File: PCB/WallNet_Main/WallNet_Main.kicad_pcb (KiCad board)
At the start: 2 copper layers, 54 parts, among them J1 Conn_01x05_Pin, J101 USB_C_Receptacle_PowerOnly_6P, J102 Conn_01x04_Pin, J201 Conn_01x04_Pin, J202 Conn_01x07_Socket, J203 Conn_02x12_Counter_Clockwise, Q201 BSS138, SW1 SW, SW201 SW, U1 BT832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

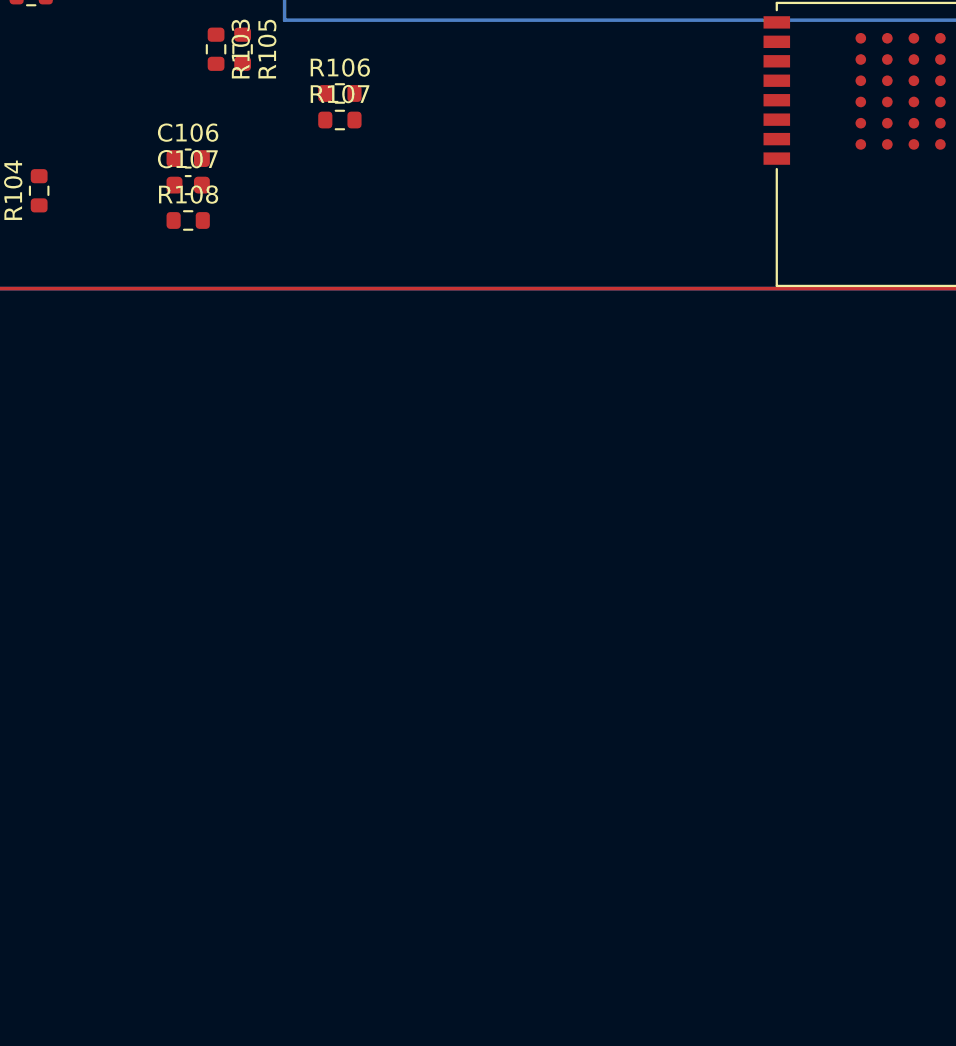
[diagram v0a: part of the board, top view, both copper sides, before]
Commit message: "added test point debugging and mounting holes"
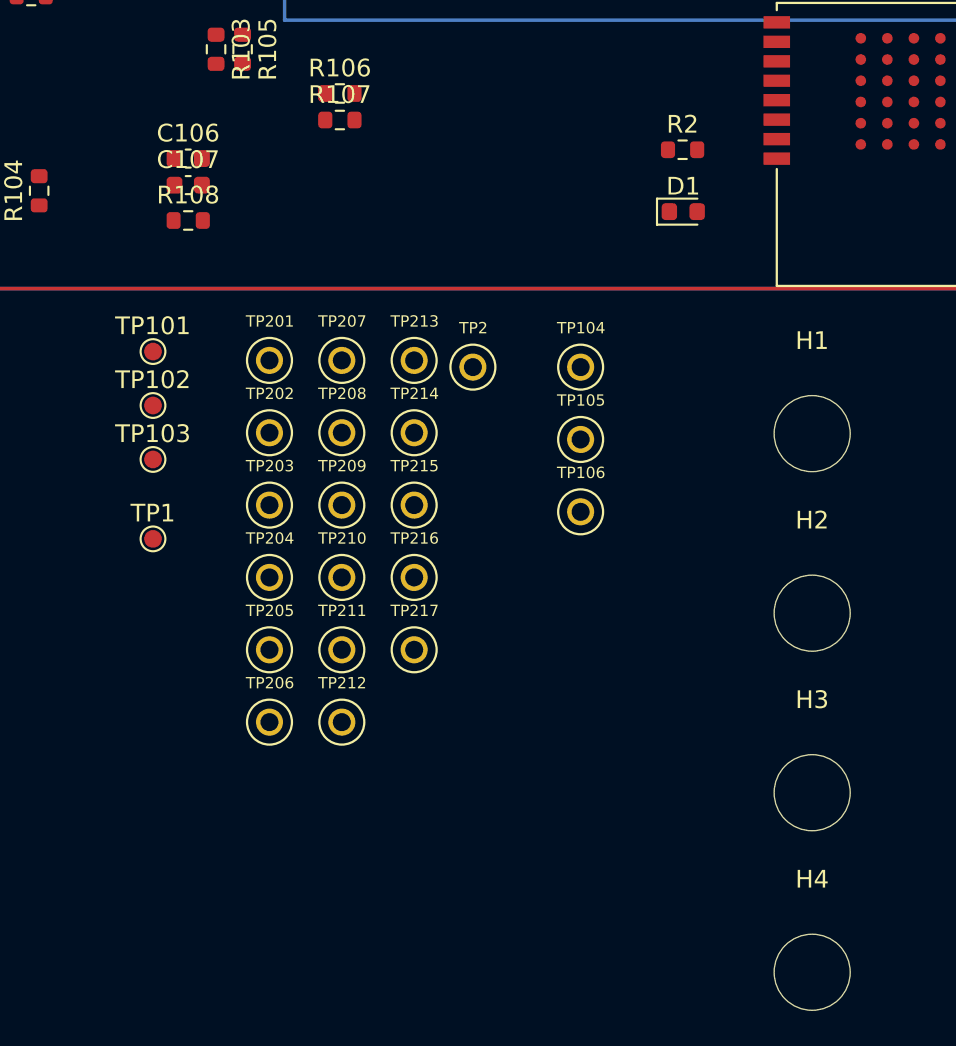
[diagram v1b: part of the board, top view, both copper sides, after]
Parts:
- added D1: LED, Diode_SMD:D_0603_1608Metric, F.Cu at (101.2, 115.5)
- added H1: MountingHole, MountingHole:MountingHole_4.3mm_M4, F.Cu at (108.5, 128.1)
- added H2: MountingHole, MountingHole:MountingHole_4.3mm_M4, F.Cu at (108.5, 138.2)
- added H3: MountingHole, MountingHole:MountingHole_4.3mm_M4, F.Cu at (108.5, 148.3)
- added H4: MountingHole, MountingHole:MountingHole_4.3mm_M4, F.Cu at (108.5, 158.5)
- added R2: 240, Resistor_SMD:R_0603_1608Metric, F.Cu at (101.2, 112.0)
- added TP1: GND, TestPoint:TestPoint_Pad_D1.0mm, F.Cu at (71.2, 134.0)
- added TP101: VBat, TestPoint:TestPoint_Pad_D1.0mm, F.Cu at (71.2, 123.4)
- added TP102: VUSB, TestPoint:TestPoint_Pad_D1.0mm, F.Cu at (71.2, 126.5)
- added TP103: VSys, TestPoint:TestPoint_Pad_D1.0mm, F.Cu at (71.2, 129.5)
- added TP104: BQ_SDA, 5001:KEYSTONE_5001, F.Cu at (95.4, 124.3)
- added TP105: BQ_SCL, 5001:KEYSTONE_5001, F.Cu at (95.4, 128.4)
- added TP106: BQ_INT, 5001:KEYSTONE_5001, F.Cu at (95.4, 132.5)
- added TP2: GND, 5001:KEYSTONE_5001, F.Cu at (89.3, 124.3)
- added TP201: TS_TX, 5001:KEYSTONE_5001, F.Cu at (77.8, 123.9)
- added TP202: TS_RX, 5001:KEYSTONE_5001, F.Cu at (77.8, 128.0)
- added TP203: GPS_SDA, 5001:KEYSTONE_5001, F.Cu at (77.8, 132.1)
- added TP204: GPS_SCL, 5001:KEYSTONE_5001, F.Cu at (77.8, 136.2)
- added TP205: GPS_INT, 5001:KEYSTONE_5001, F.Cu at (77.8, 140.3)
- added TP206: GPS_TP, 5001:KEYSTONE_5001, F.Cu at (77.8, 144.4)
- added TP207: RFID_RST, 5001:KEYSTONE_5001, F.Cu at (81.9, 123.9)
- added TP208: RFID_SCK, 5001:KEYSTONE_5001, F.Cu at (81.9, 128.0)
- added TP209: RFID_MISO, 5001:KEYSTONE_5001, F.Cu at (81.9, 132.1)
- added TP210: RFID_MOSI, 5001:KEYSTONE_5001, F.Cu at (81.9, 136.2)
- added TP211: RFID_SS, 5001:KEYSTONE_5001, F.Cu at (81.9, 140.3)
- added TP212: EP_DC, 5001:KEYSTONE_5001, F.Cu at (81.9, 144.4)
- added TP213: EP_SDA, 5001:KEYSTONE_5001, F.Cu at (86.0, 123.9)
- added TP214: EP_SCL, 5001:KEYSTONE_5001, F.Cu at (86.0, 128.0)
- added TP215: EP_CSB, 5001:KEYSTONE_5001, F.Cu at (86.0, 132.1)
- added TP216: EP_BUSY, 5001:KEYSTONE_5001, F.Cu at (86.0, 136.2)
- added TP217: EP_RESET, 5001:KEYSTONE_5001, F.Cu at (86.0, 140.3)
- R109: value UNKNOWN -> 240

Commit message: Updated, Schematic done, waiting on Layout
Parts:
- removed SW201: SW, 436331045822:4363X10458XX
- added L101: 2.2uH, ISMC:IND_IMSC1008AZER_VIS, F.Cu at (46.2, 91.4)
- added L201: 68uH, VLS3015CX_680M_H:IND_VLS3015CX-680M-H, F.Cu at (184.2, 74.8)
- added S201: 436331045822, 436331045822:4363X10458XX, F.Cu at (156.8, 66.2)
- moved TP211 188.4 mm to (239.9, 37.6)
- moved TP210 182.0 mm to (234.9, 37.6)
- moved TP209 175.2 mm to (229.4, 37.6)
- moved TP208 168.3 mm to (223.9, 37.6)
- moved H2 165.6 mm to (274.0, 133.5)
- moved H3 165.5 mm to (274.0, 146.3)
- moved H4 165.5 mm to (274.0, 156.5)
- moved H1 165.2 mm to (273.5, 120.0)
- moved TP207 161.9 mm to (218.9, 37.6)
- moved TP206 153.5 mm to (190.9, 40.6)
- moved TP205 147.4 mm to (186.4, 40.6)
- moved TP204 141.3 mm to (181.9, 40.6)
- moved TP212 138.7 mm to (205.2, 80.8)
- moved TP203 135.2 mm to (177.4, 40.6)
- moved C202 129.8 mm to (193.2, 55.2)
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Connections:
- J102 pad MP: (no net) -> GND
- J201 pad MP: (no net) -> GND
- J203 pad MP: (no net) -> GND

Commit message: Placed components on board
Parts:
- moved H4 292.0 mm to (17.5, 17.0)
- moved H3 265.8 mm to (17.5, 76.5)
- moved TP211 220.9 mm to (19.5, 52.0)
- moved J202 219.1 mm to (20.8, 56.0), turned to 0 degrees
- moved TP210 215.0 mm to (24.0, 79.5)
- moved TP209 208.9 mm to (24.0, 75.5)
- moved TP208 200.3 mm to (28.0, 79.5)
- moved TP207 199.7 mm to (19.5, 48.5)
- moved U201 178.6 mm to (67.5, 17.0)
- moved H1 178.3 mm to (128.0, 17.0)
- moved H2 156.7 mm to (128.0, 76.5)
- moved C1 128.6 mm to (25.3, 15.0), turned to 180 degrees
- moved C3 124.5 mm to (25.9, 17.8), turned to 180 degrees
- moved D1 121.6 mm to (29.8, 15.0), turned to 180 degrees
- moved R2 117.2 mm to (29.8, 18.5), turned to 180 degrees
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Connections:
- J102 pad MP: GND -> (no net)
- J201 pad MP: GND -> (no net)
- J203 pad MP: GND -> (no net)

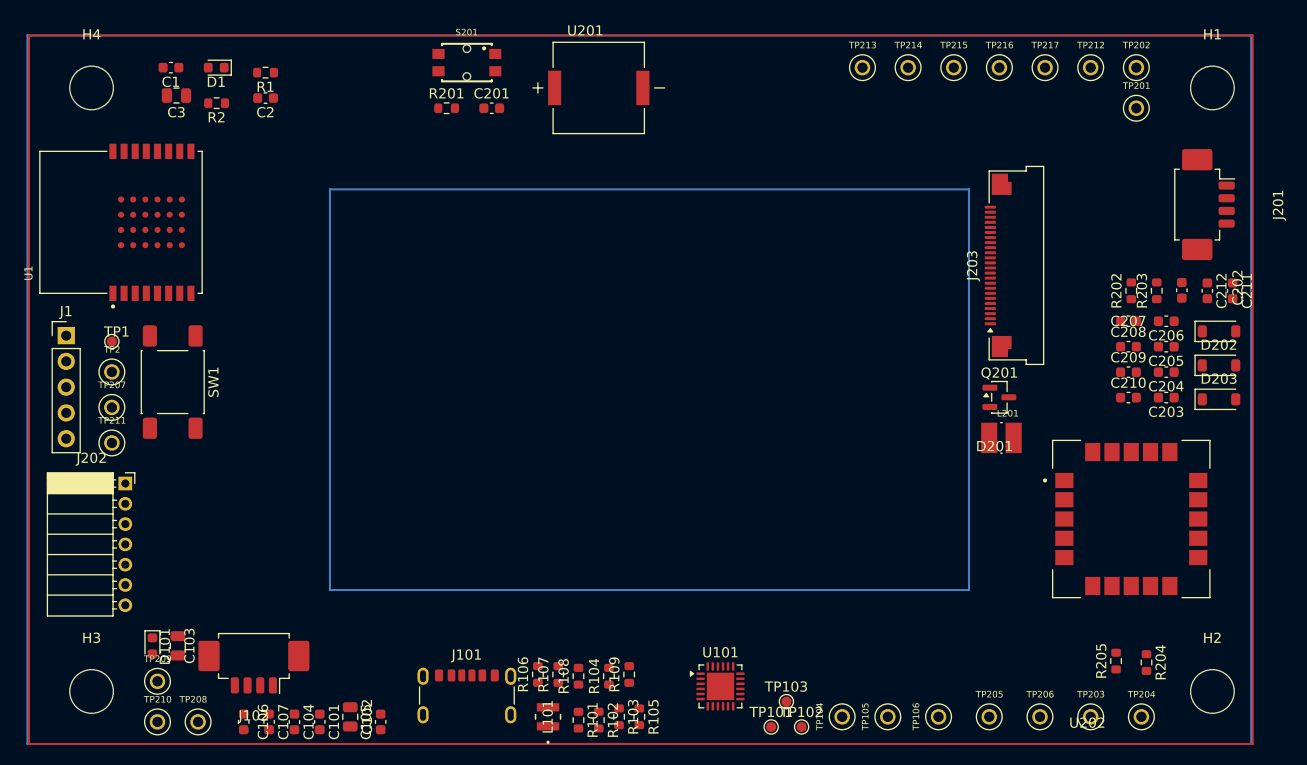
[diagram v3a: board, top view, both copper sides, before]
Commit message: Added some of the power traces
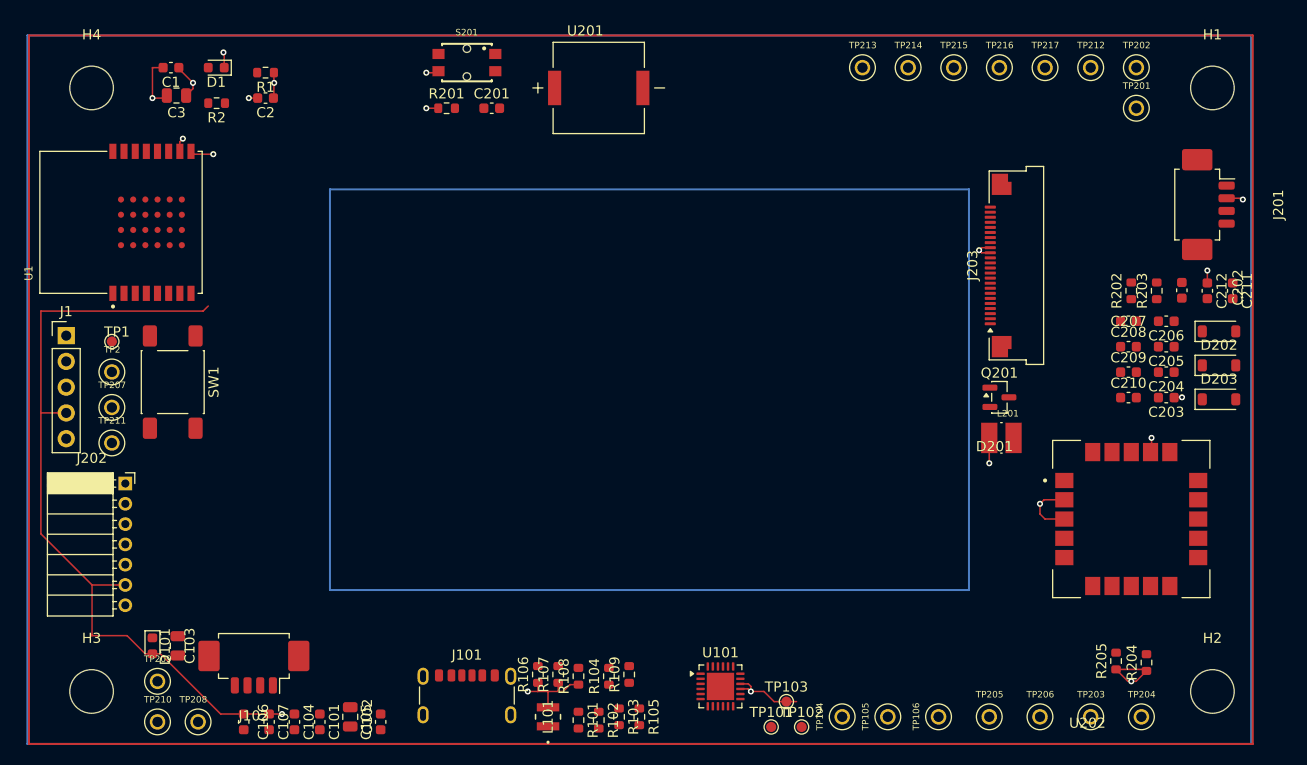
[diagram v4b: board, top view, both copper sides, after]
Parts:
- turned R204 to 90 degrees
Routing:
- net VDD_nrf: track 0.00 -> 356.4 mm, vias 0 -> 15
- net GND: track 0.00 -> 56.0 mm, vias 0 -> 5
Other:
- copper layers 2 -> 4

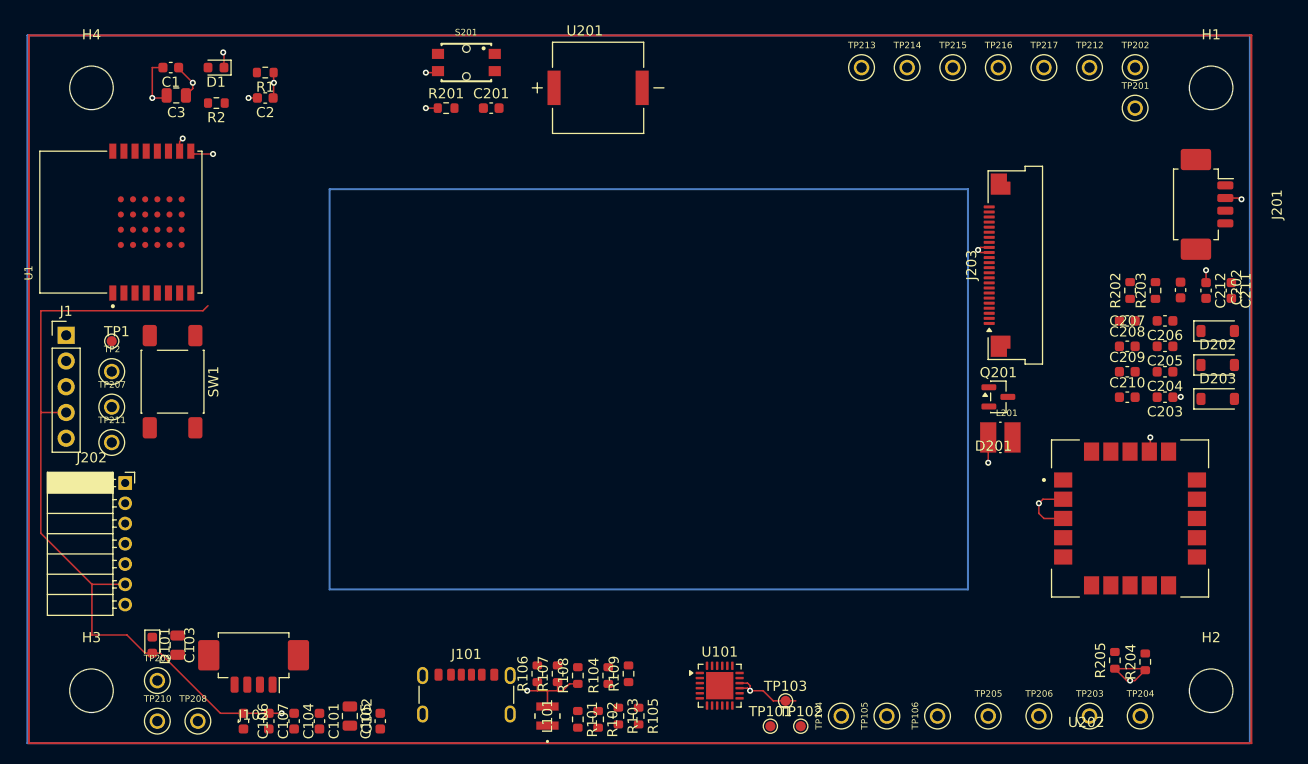
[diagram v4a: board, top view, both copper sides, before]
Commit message: Added more traces for power
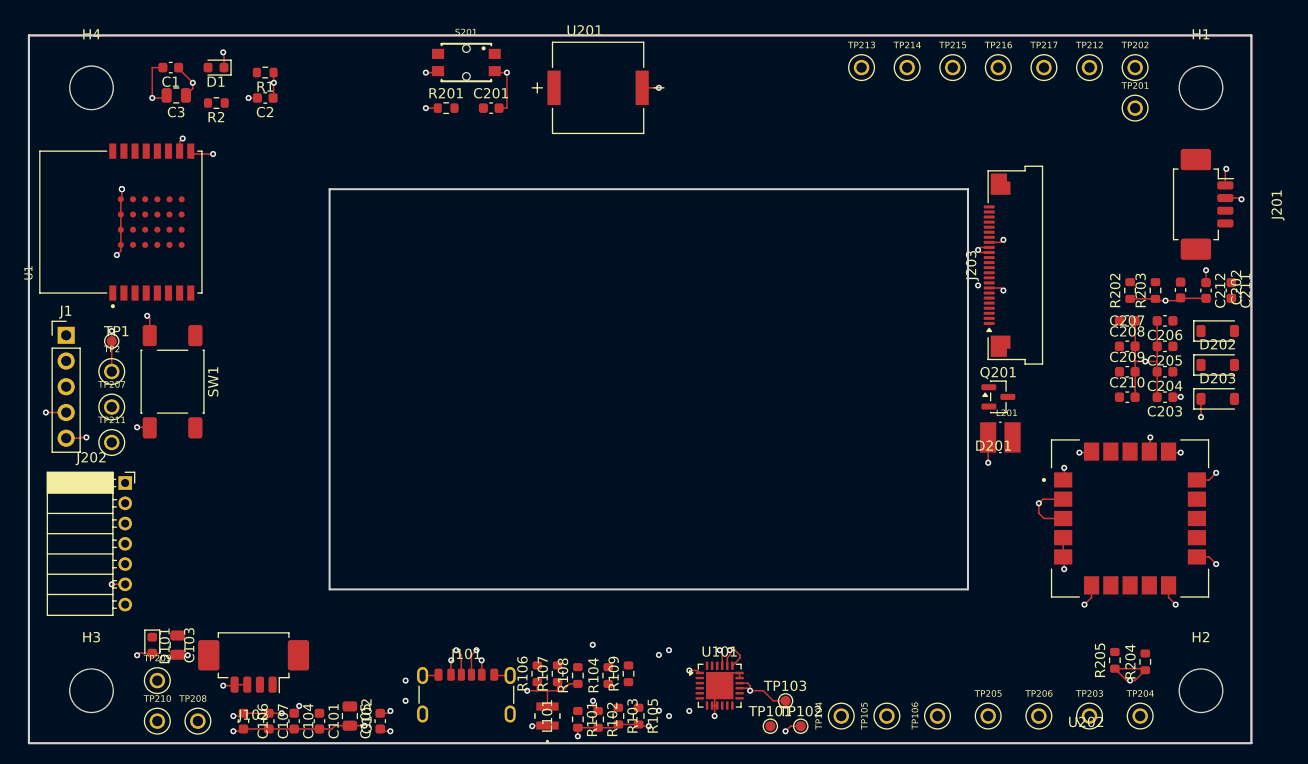
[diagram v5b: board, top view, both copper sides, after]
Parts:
- moved H1 1.00 mm to (127.0, 17.0)
- moved H2 1.00 mm to (127.0, 76.5)
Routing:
- net /Battery/VBUS_BQ: track 0.00 -> 63.8 mm, vias 0 -> 8
- net GND: track 56.0 -> 116.0 mm, vias 5 -> 35
- net /Battery/SW: track 0.00 -> 48.3 mm, vias 0 -> 5
- net /Battery/BTST: track 0.00 -> 43.4 mm, vias 0 -> 4
- net Net-(J101-CC1): track 0.00 -> 23.1 mm, vias 0 -> 3
- net VDD_nrf: track 356.4 -> 370.8 mm, vias 15 -> 20
- net Net-(J101-CC2): track 0.00 -> 2.63 mm, vias 0 -> 1
- added copper zone on In2.Cu, net GND
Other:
- board outline added: 120.6 x 69.8 mm

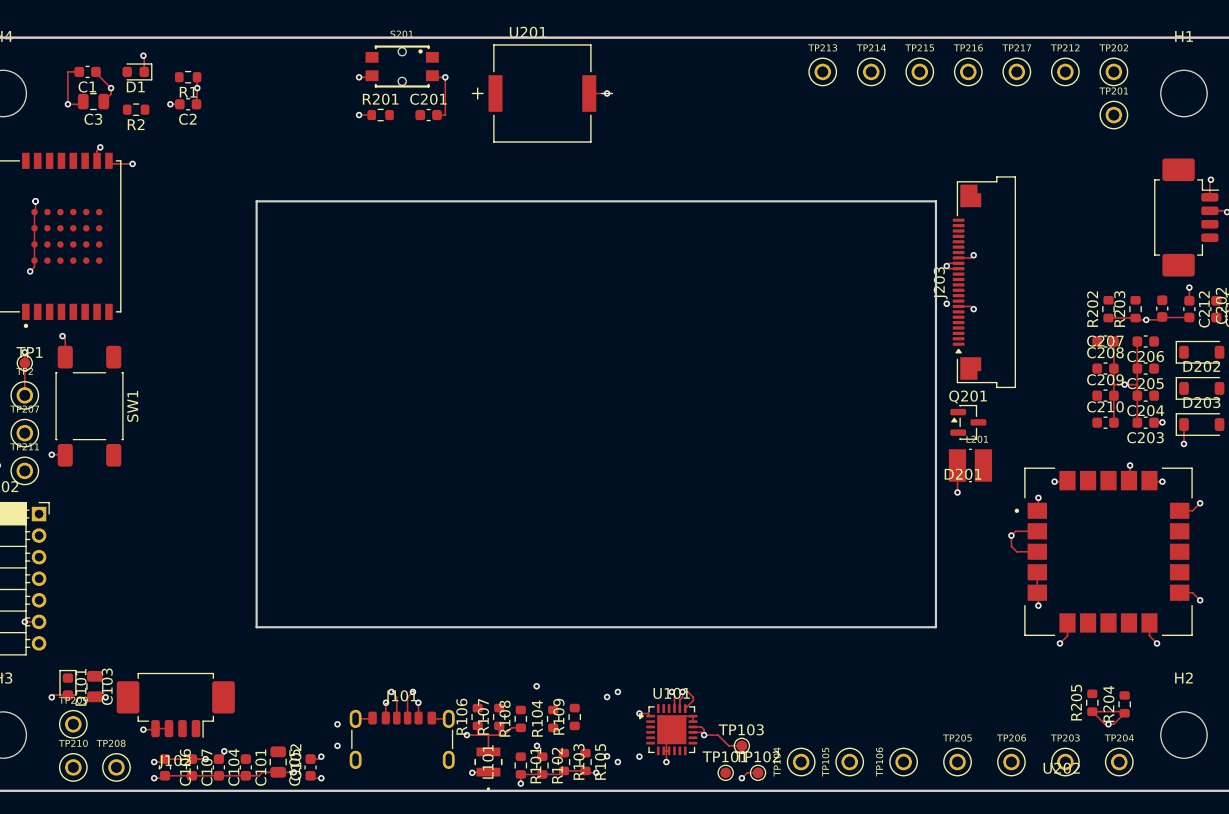
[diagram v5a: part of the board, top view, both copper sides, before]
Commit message: Finished wiring up BMU/PWR system
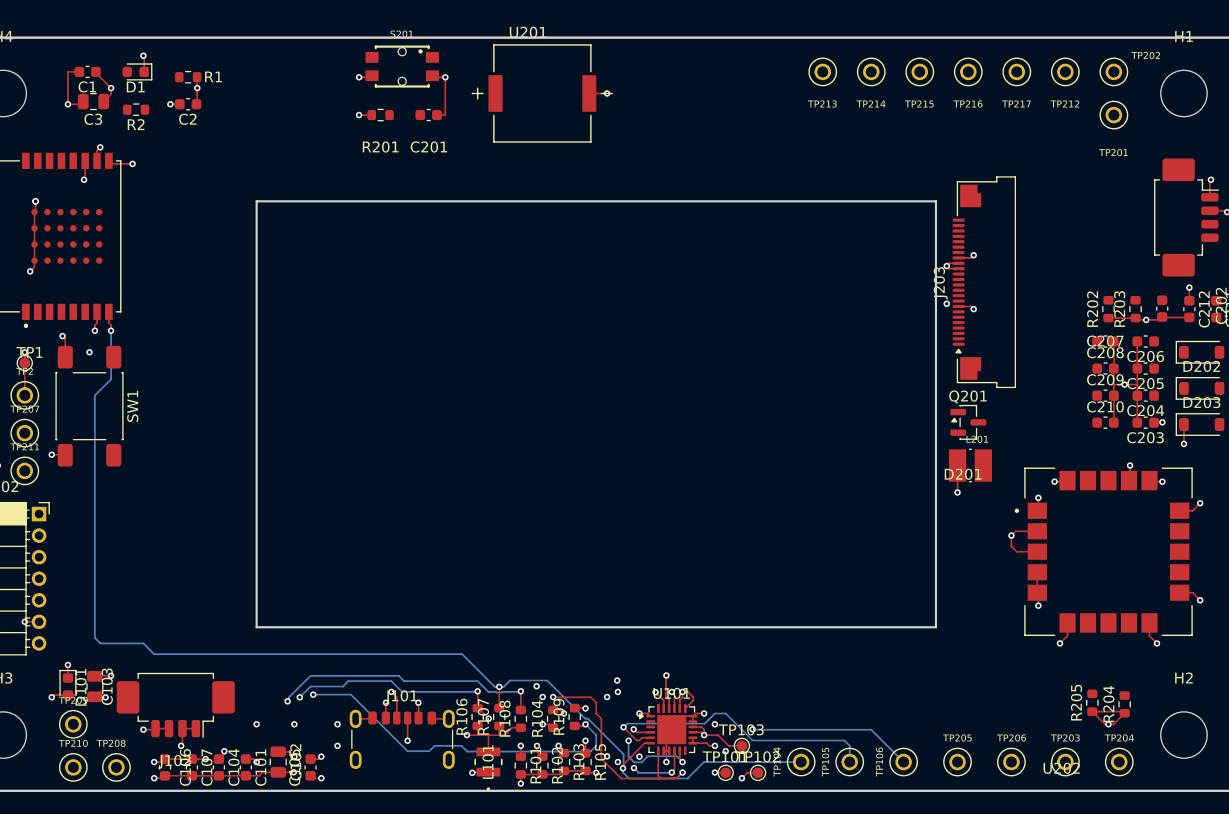
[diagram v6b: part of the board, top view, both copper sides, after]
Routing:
- net /P13: track 0.00 -> 144.2 mm, vias 0 -> 8
- net /P09: track 0.00 -> 124.2 mm, vias 0 -> 5
- net /P10: track 0.00 -> 109.7 mm, vias 0 -> 3
- net /Battery/BAT: track 0.00 -> 80.7 mm, vias 0 -> 5
- net Net-(D101-K): track 0.00 -> 60.9 mm, vias 0 -> 3
- net /Battery/REGN: track 0.00 -> 52.1 mm, vias 0 -> 5
- net /Battery/PMID: track 0.00 -> 42.6 mm, vias 0 -> 4
- net /Battery/TS: track 0.00 -> 18.8 mm, vias 0 -> 4
- net /Battery/ILIM: track 0.00 -> 15.4 mm, vias 0 -> 3
- net Net-(J101-CC2): track 2.63 -> 13.8 mm, vias 1 -> 2
- net /Battery/STAT: track 0.00 -> 7.99 mm, vias 0 -> 2
- net GND: track 116.0 -> 117.2 mm, vias 35 -> 36
